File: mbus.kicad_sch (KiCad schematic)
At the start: 32 parts, among them J1 USB_C_Receptacle_USB2.0, J2 MBUS, Q1 BC817, Q2 BC817, Q3 BC807, U1 AP3015, U2 USBLC6-2SC6, U3 CH340E

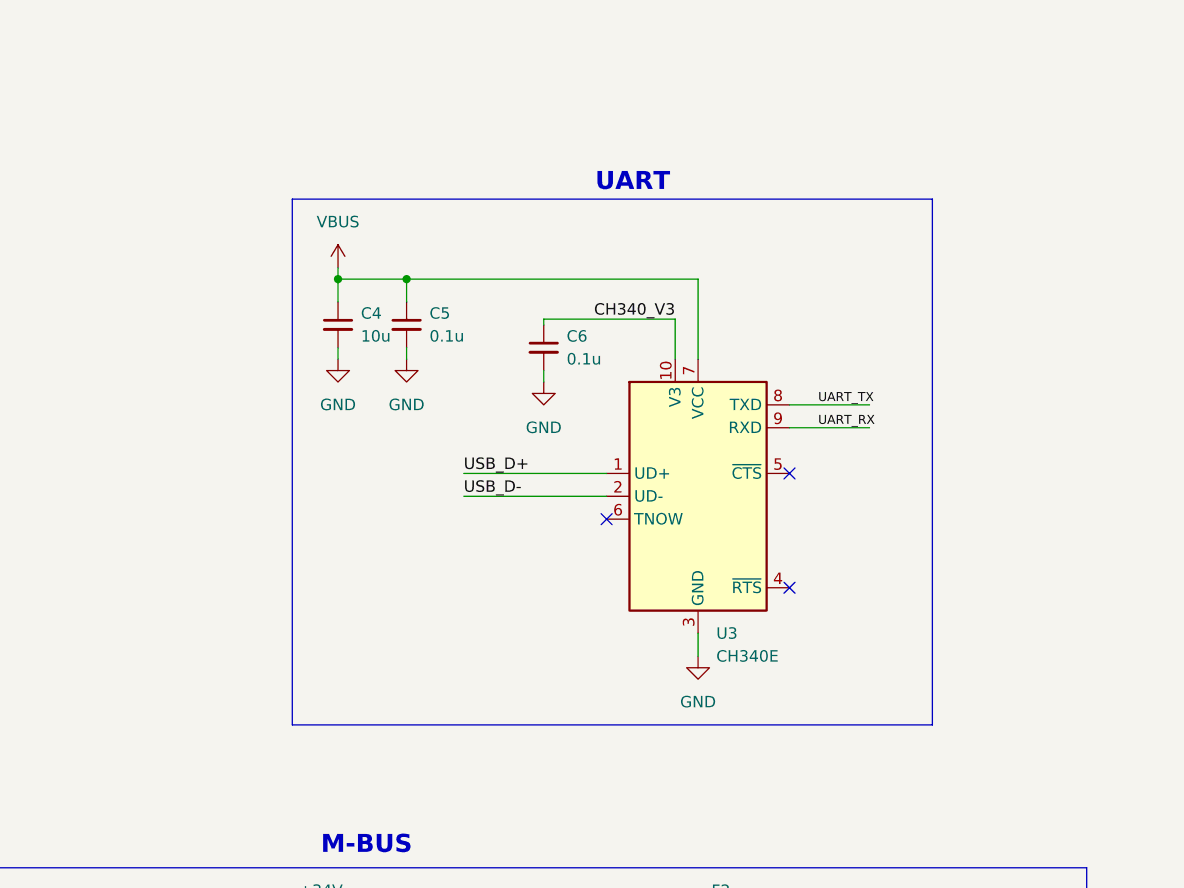
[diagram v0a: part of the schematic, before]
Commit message: Added mounting holes, board outline done
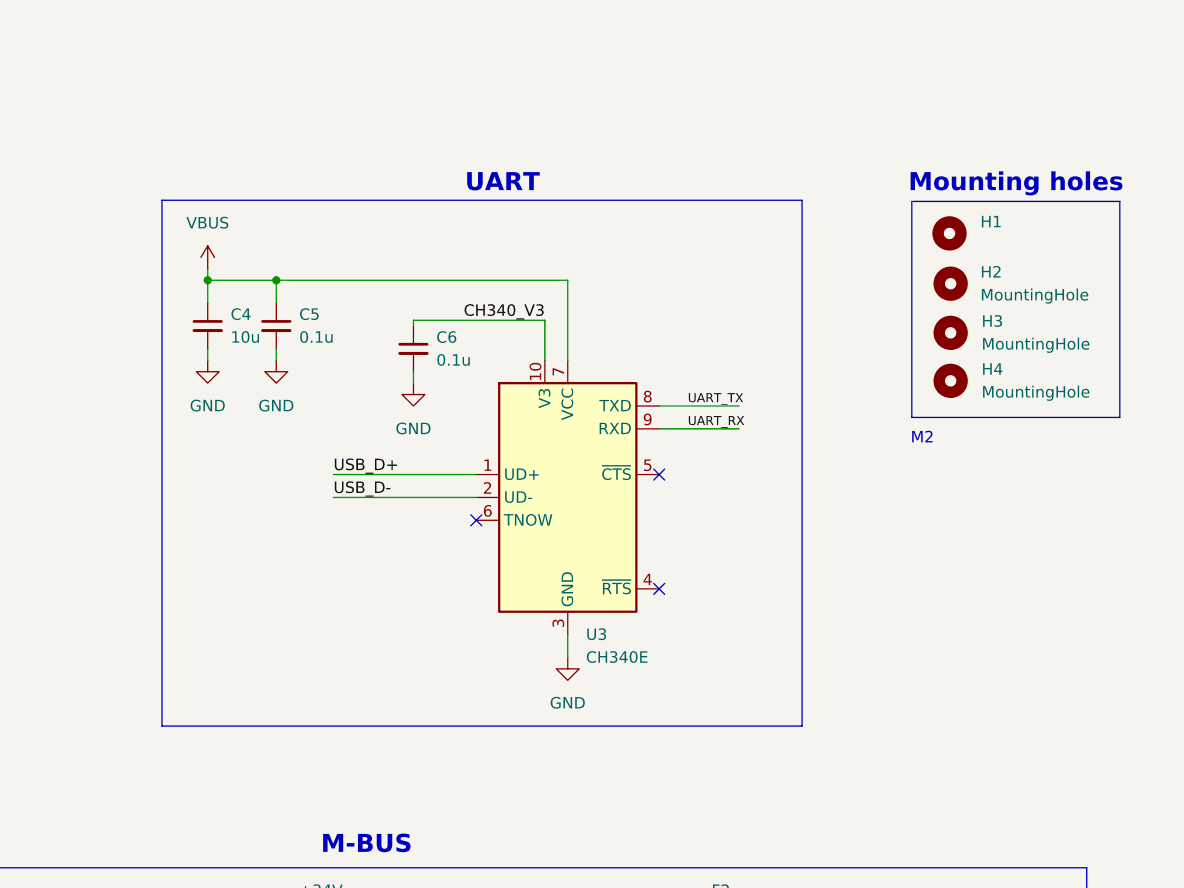
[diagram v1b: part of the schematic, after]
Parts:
- added H1: (no value), symbol Mechanical:MountingHole
- added H2, H3, H4: MountingHole, MountingHole:MountingHole_2.2mm_M2, symbol Mechanical:MountingHole
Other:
- note added: "M2"
- note added: "Mounting holes"
- moved on the sheet: C4, C5, C6, U3

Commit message: PCB rev0.1 finished
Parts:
- H1: value (none) -> MountingHole; footprint (none) -> MountingHole:MountingHole_2.2mm_M2
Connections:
- net BOOST_OUT: now reaches D1.2 (A), L1.2, U1.1 (SW)
- net BOOST_FB: now reaches R3.2, R4.1, U1.3 (FB)
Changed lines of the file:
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@@
     (effects (font (size 4 4) (thickness 0.8) bold) (justify left bottom))
+  )
+  (label "BOOST_FB" (at 70.993 147.955 0)
+    (effects (font (size 1.27 1.27)) (justify left bottom))
   )
   (label "UART_TX" (at 227.457 57.912 0)
@@
   )
   (label "USB_D+" (at 188.087 65.532 0)
+    (effects (font (size 1.27 1.27)) (justify left bottom))
+  )
+  (label "BOOST_OUT" (at 73.025 142.875 0)
     (effects (font (size 1.27 1.27)) (justify left bottom))
   )
@@
       (effects (font (size 1.27 1.27)) (justify left))
     )
-    (property "Value" "" (id 1) (at 259.969 40.0049 0)
-      (effects (font (size 1.27 1.27)) (justify left))
-    )
-    (property "Footprint" "" (id 2) (at 256.54 38.735 0)
-      (effects (font (size 1.27 1.27)) hide)
-    )
+    (property "Value" "MountingHole" (id 1) (at 259.969 40.0049 0)
+      (effects (font (size 1.27 1.27)) (justify left))
+    )
+    (property "Footprint" "MountingHole:MountingHole_2.2mm_M2" (id 2) (at 256.54 38.735 0)
+      (effects (font (size 1.27 1.27)) hide)
+    )

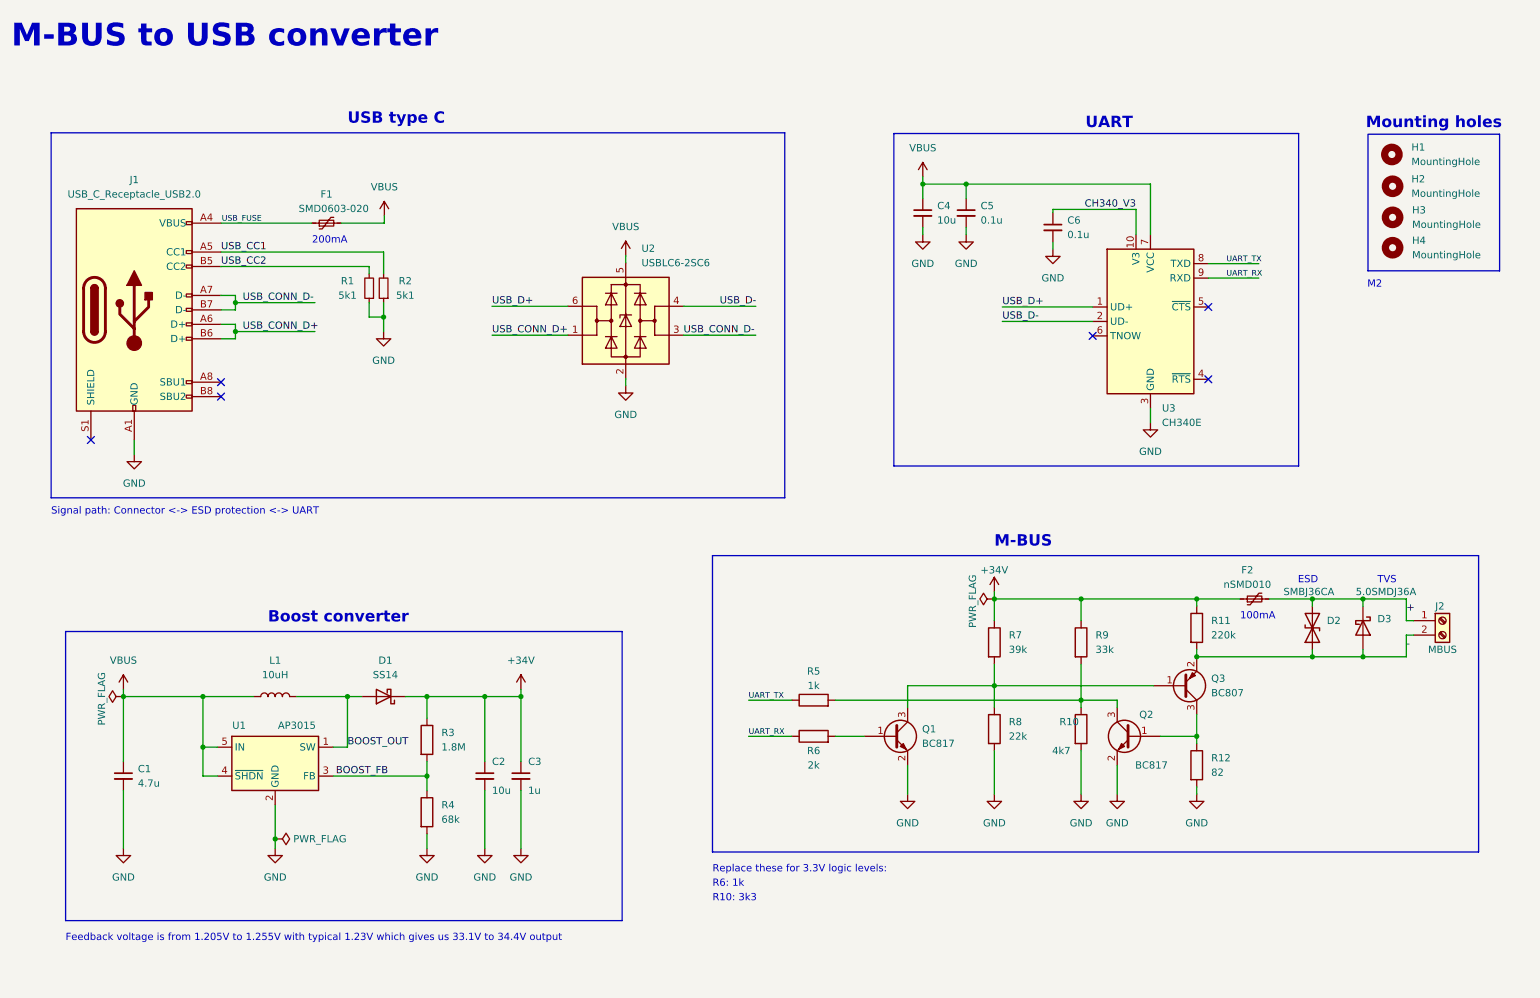
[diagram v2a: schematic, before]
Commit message: Fixed LCSC part IDs
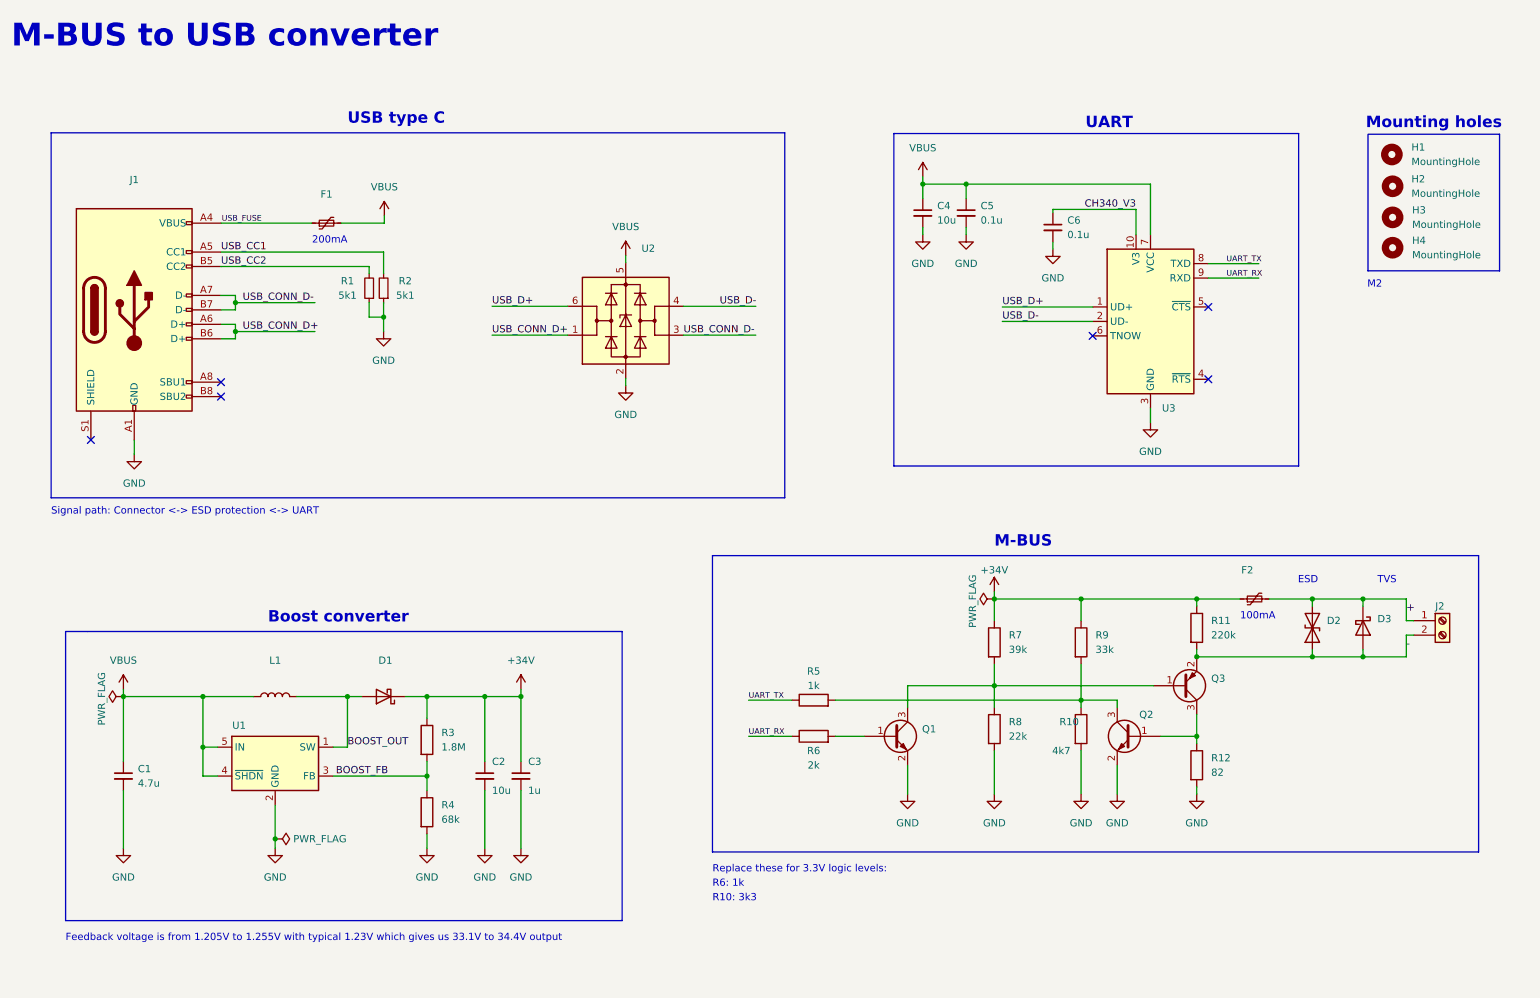
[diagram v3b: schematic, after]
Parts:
- D1: value SS14 -> (none); footprint Diode_SMD:D_SOD-123F -> (none); LCSC C190475 -> (none); LCSC Part (none) -> C190475
- D2: value SMBJ36CA -> (none); footprint Diode_SMD:D_SMB -> (none); LCSC C83326 -> (none); LCSC Part (none) -> C83326
- D3: value 5.0SMDJ36A -> (none); footprint Diode_SMD:D_SMC -> (none); LCSC C522690 -> (none); LCSC Part (none) -> C522690
- F1: value SMD0603-020 -> (none); footprint Fuse:Fuse_0603_1608Metric -> (none); LCSC C2760255 -> (none); LCSC Part (none) -> C2760255
- F2: value nSMD010 -> (none); footprint Fuse:Fuse_1206_3216Metric -> (none); LCSC C70065 -> (none); LCSC Part (none) -> C70065
- J1: value USB_C_Receptacle_USB2.0 -> (none); footprint Connector_USB:USB_C_Receptacle_HRO_TYPE-C-31-M-12 -> (none); LCSC Part (none) -> C165948
- J2: value MBUS -> (none); footprint TerminalBlock_Phoenix:TerminalBlock_Phoenix_PT-1,5-2-5.0-H_1x02_P5.00mm_Horizontal -> (none); LCSC C474881 -> (none); LCSC Part (none) -> C474881
- L1: value 10uH -> (none); footprint Inductor_SMD:L_Sunlord_MWSA0518_5.4x5.2mm -> (none); LCSC C408412 -> (none); LCSC Part (none) -> C408412
- Q1, Q2: value BC817 -> (none); footprint Package_TO_SOT_SMD:SOT-23 -> (none); LCSC C604682 -> (none); LCSC Part (none) -> C604682
- Q3: value BC807 -> (none); footprint Package_TO_SOT_SMD:SOT-23 -> (none); LCSC C82369 -> (none); LCSC Part (none) -> C82369
- U1: value AP3015 -> (none); footprint Package_TO_SOT_SMD:SOT-23-5 -> (none); LCSC C151334 -> (none); LCSC Part (none) -> C151334
- U2: value USBLC6-2SC6 -> (none); footprint Package_TO_SOT_SMD:SOT-23-6 -> (none); LCSC C2827654 -> (none); LCSC Part (none) -> C2827654
- U3: value CH340E -> (none); footprint Package_SO:MSOP-10_3x3mm_P0.5mm -> (none); LCSC C99652 -> (none); LCSC Part (none) -> C99652

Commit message: Added CH340N symbol just in case, added part numbers for the rest of the passive components
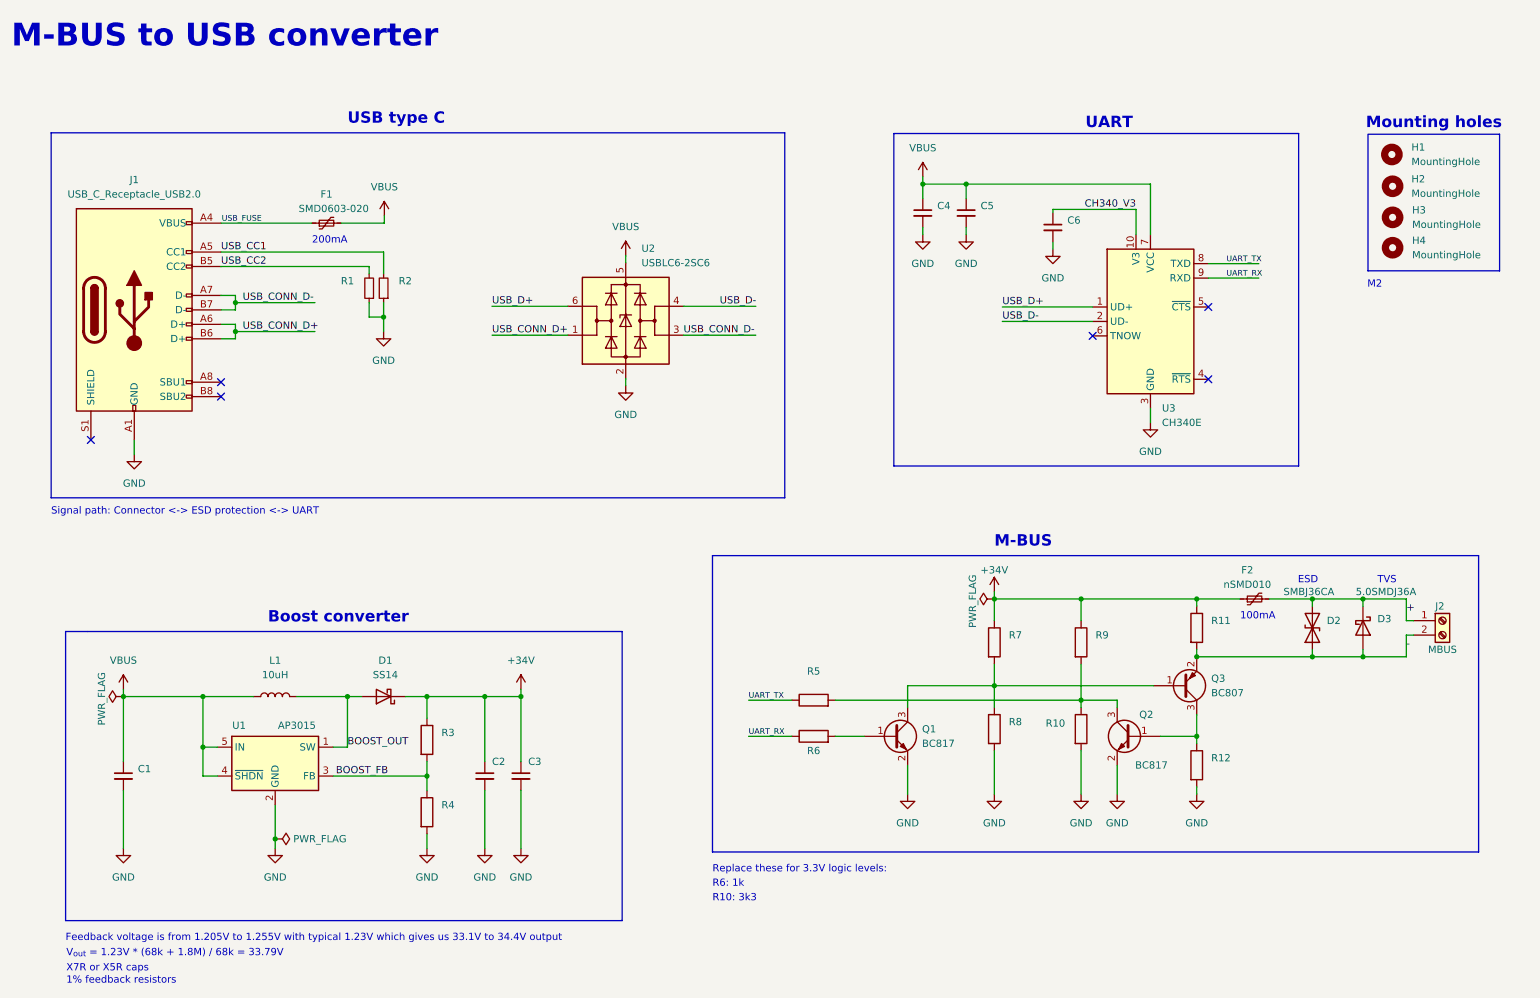
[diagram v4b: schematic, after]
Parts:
- C1: value 4.7u -> (none); footprint Capacitor_SMD:C_0603_1608Metric -> (none); LCSC Part (none) -> C1705
- C2: value 10u -> (none); footprint Capacitor_SMD:C_0603_1608Metric -> (none); LCSC Part (none) -> C2911377
- C3: value 1u -> (none); footprint Capacitor_SMD:C_0603_1608Metric -> (none); LCSC Part (none) -> C77386
- C4: value 10u -> (none); footprint Capacitor_SMD:C_0402_1005Metric -> (none); LCSC Part (none) -> C15525
- C5, C6: value 0.1u -> (none); footprint Capacitor_SMD:C_0402_1005Metric -> (none); LCSC Part (none) -> C169292
- D1: value (none) -> SS14; footprint (none) -> Diode_SMD:D_SOD-123F
- D2: value (none) -> SMBJ36CA; footprint (none) -> Diode_SMD:D_SMB
- D3: value (none) -> 5.0SMDJ36A; footprint (none) -> Diode_SMD:D_SMC
- F1: value (none) -> SMD0603-020; footprint (none) -> Fuse:Fuse_0603_1608Metric
- F2: value (none) -> nSMD010; footprint (none) -> Fuse:Fuse_1206_3216Metric
- J1: value (none) -> USB_C_Receptacle_USB2.0; footprint (none) -> Connector_USB:USB_C_Receptacle_HRO_TYPE-C-31-M-12
- J2: value (none) -> MBUS; footprint (none) -> TerminalBlock_Phoenix:TerminalBlock_Phoenix_PT-1,5-2-5.0-H_1x02_P5.00mm_Horizontal
- L1: value (none) -> 10uH; footprint (none) -> Inductor_SMD:L_Sunlord_MWSA0518_5.4x5.2mm
- Q1, Q2: value (none) -> BC817; footprint (none) -> Package_TO_SOT_SMD:SOT-23
- Q3: value (none) -> BC807; footprint (none) -> Package_TO_SOT_SMD:SOT-23
- R1, R2: value 5k1 -> (none); footprint Resistor_SMD:R_0402_1005Metric -> (none); LCSC Part (none) -> C203181
- R10: value 4k7 -> (none); footprint Resistor_SMD:R_0603_1608Metric -> (none); LCSC Part (none) -> C441894
- R11: value 220k -> (none); footprint Resistor_SMD:R_0603_1608Metric -> (none); LCSC Part (none) -> C441934
- R12: value 82 -> (none); footprint Resistor_SMD:R_0603_1608Metric -> (none); LCSC Part (none) -> C445805
- R3: value 1.8M -> (none); footprint Resistor_SMD:R_0603_1608Metric -> (none); LCSC Part (none) -> C177951
- R4: value 68k -> (none); footprint Resistor_SMD:R_0603_1608Metric -> (none); LCSC Part (none) -> C667733
- R5: value 1k -> (none); footprint Resistor_SMD:R_0603_1608Metric -> (none); LCSC Part (none) -> C966204
- R6: value 2k -> (none); footprint Resistor_SMD:R_0603_1608Metric -> (none); LCSC Part (none) -> C445827
- R7: value 39k -> (none); footprint Resistor_SMD:R_0603_1608Metric -> (none); LCSC Part (none) -> C118370
- R8: value 22k -> (none); footprint Resistor_SMD:R_0603_1608Metric -> (none); LCSC Part (none) -> C441928
- R9: value 33k -> (none); footprint Resistor_SMD:R_0603_1608Metric -> (none); LCSC Part (none) -> C441899
- U1: value (none) -> AP3015; footprint (none) -> Package_TO_SOT_SMD:SOT-23-5
- U2: value (none) -> USBLC6-2SC6; footprint (none) -> Package_TO_SOT_SMD:SOT-23-6
- U3: value (none) -> CH340E; footprint (none) -> Package_SO:MSOP-10_3x3mm_P0.5mm
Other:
- note added: "1% feedback resistors"
- note added: "V_{out} = 1.23V * (68k + 1.8M) / 68k = 33.79V"
- note added: "X7R or X5R caps"
